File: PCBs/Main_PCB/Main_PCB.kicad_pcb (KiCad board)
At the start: 2 copper layers, 70 x 56 mm, 12 parts, among them J1 LIGHT, J2 OLED, J3 BUTTONS, J4 USB1, J5 USB2, Q1 2N3904, Q2 2N3904, U1 Pico, U2 DS1302, Y1 32.768 KHz

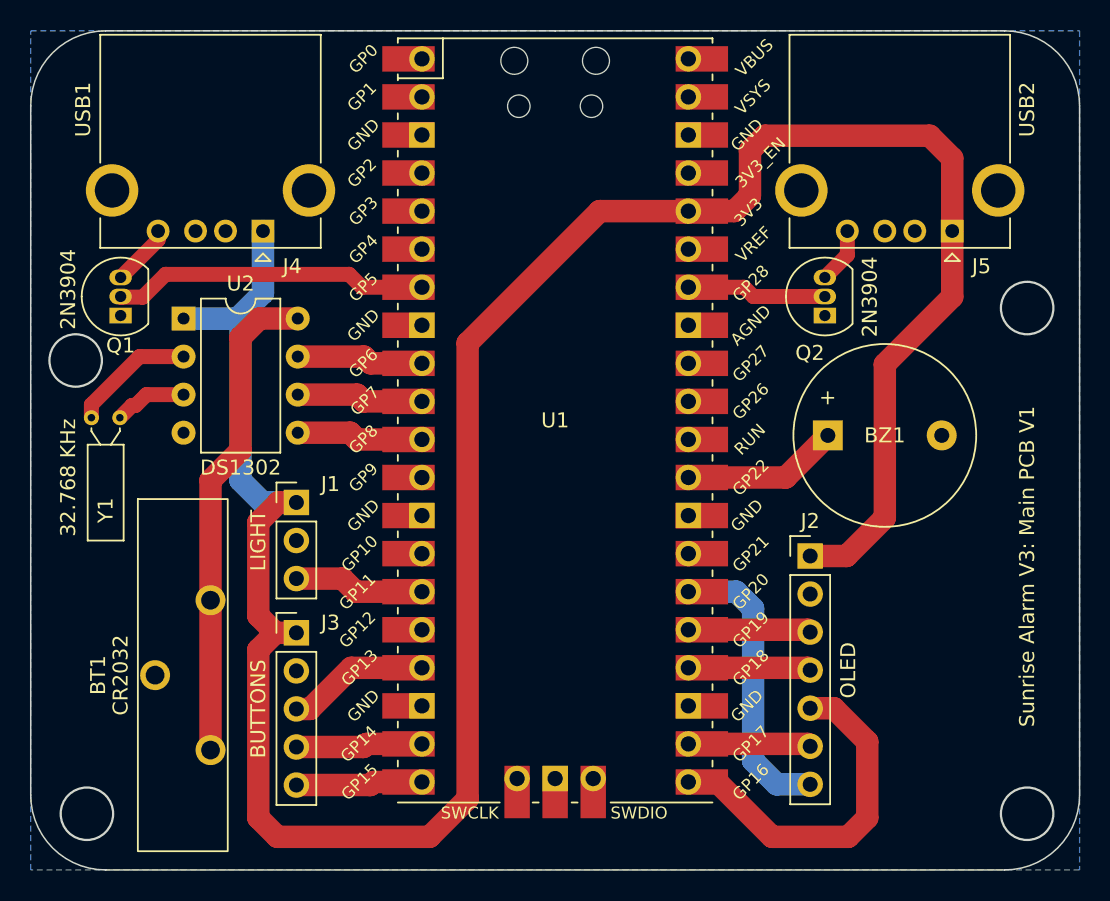
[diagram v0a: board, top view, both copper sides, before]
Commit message: V3.4.1-alpha Added PCB Labels
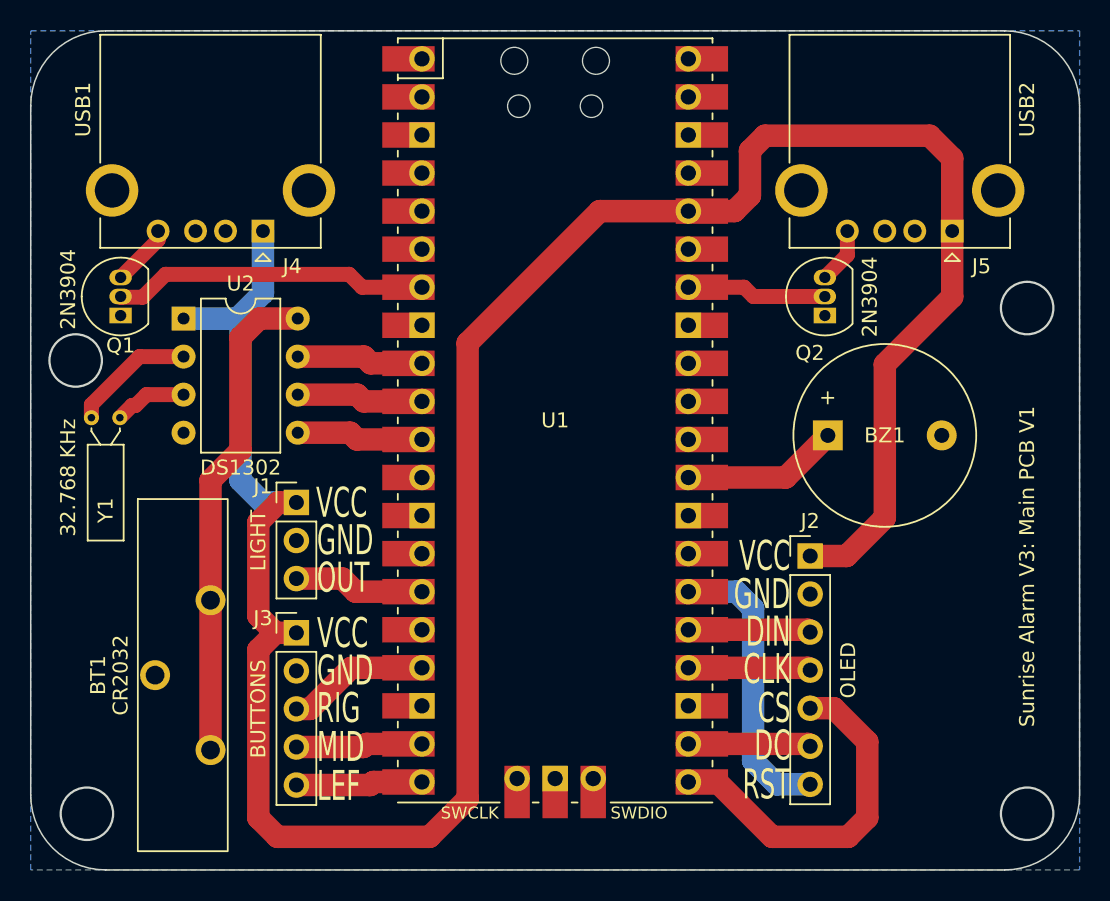
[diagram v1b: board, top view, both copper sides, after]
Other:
- board text added: "CLK"
- board text added: "CS"
- board text added: "DC"
- board text added: "DIN"
- board text added: "GND"
- board text added: "LEF"
- board text added: "MID"
- board text added: "OUT"
- board text added: "RIG"
- board text added: "RST"
- board text added: "VCC"
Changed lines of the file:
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@@
     (property "Sheetname" "")
     (attr through_hole)
-    (fp_text reference "J3" (at 2.27 -0.675) (layer "F.SilkS")
+    (fp_text reference "J3" (at -2.23 -0.975) (layer "F.SilkS")
       (effects (font (size 1 1) (thickness 0.15)))
     )
@@
       (effects (font (size 1 1) (thickness 0.15)))
     )
-    (fp_text user "GP15" (at -13.054 24.13 45) (layer "F.SilkS")
-      (effects (font (size 0.8 0.8) (thickness 0.15)))
-    )
-    (fp_text user "GND" (at 12.8 -19.05 45) (layer "F.SilkS")
-      (effects (font (size 0.8 0.8) (thickness 0.15)))
-    )
-    (fp_text user "GP4" (at -12.8 -11.43 45) (layer "F.SilkS")
-      (effects (font (size 0.8 0.8) (thickness 0.15)))
-    )
-    (fp_text user "GND" (at 12.8 19.05 45) (layer "F.SilkS")
-      (effects (font (size 0.8 0.8) (thickness 0.15)))
-    )
-    (fp_text user "GP28" (at 13.054 -9.144 45) (layer "F.SilkS")
-      (effects (font (size 0.8 0.8) (thickness 0.15)))
-    )
-    (fp_text user "GP18" (at 13.054 16.51 45) (layer "F.SilkS")
-      (effects (font (size 0.8 0.8) (thickness 0.15)))
-    )
-    (fp_text user "RUN" (at 13 1.27 45) (layer "F.SilkS")
-      (effects (font (size 0.8 0.8) (thickness 0.15)))
-    )
-    (fp_text user "GP9" (at -12.8 3.81 45) (layer "F.SilkS")
-      (effects (font (size 0.8 0.8) (thickness 0.15)))
-    )
-    (fp_text user "GP7" (at -12.7 -1.3 45) (layer "F.SilkS")
-      (effects (font (size 0.8 0.8) (thickness 0.15)))
-    )
     (fp_text user "SWDIO" (at 5.6 26.2) (layer "F.SilkS")
       (effects (font (size 0.8 0.8) (thickness 0.15)))
     )
-    (fp_text user "3V3" (at 12.9 -13.9 45) (layer "F.SilkS")
-      (effects (font (size 0.8 0.8) (thickness 0.15)))
-    )
-    (fp_text user "GP27" (at 13.054 -3.8 45) (layer "F.SilkS")
-      (effects (font (size 0.8 0.8) (thickness 0.15)))
-    )
-    (fp_text user "GP22" (at 13.054 3.81 45) (layer "F.SilkS")
-      (effects (font (size 0.8 0.8) (thickness 0.15)))
-    )
-    (fp_text user "GP21" (at 13.054 8.9 45) (layer "F.SilkS")
-      (effects (font (size 0.8 0.8) (thickness 0.15)))
-    )
-    (fp_text user "GP8" (at -12.8 1.27 45) (layer "F.SilkS")
-      (effects (font (size 0.8 0.8) (thickness 0.15)))
-    )
-    (fp_text user "GP5" (at -12.8 -8.89 45) (layer "F.SilkS")
-      (effects (font (size 0.8 0.8) (thickness 0.15)))
-    )
-    (fp_text user "GP20" (at 13.054 11.43 45) (layer "F.SilkS")
-      (effects (font (size 0.8 0.8) (thickness 0.15)))
-    )
-    (fp_text user "GP14" (at -13.1 21.59 45) (layer "F.SilkS")
-      (effects (font (size 0.8 0.8) (thickness 0.15)))
-    )
-    (fp_text user "GND" (at -12.8 -6.35 45) (layer "F.SilkS")
-      (effects (font (size 0.8 0.8) (thickness 0.15)))
-    )
-    (fp_text user "GND" (at -12.8 19.05 45) (layer "F.SilkS")
-      (effects (font (size 0.8 0.8) (thickness 0.15)))
-    )
-    (fp_text user "GP26" (at 13.054 -1.27 45) (layer "F.SilkS")
-      (effects (font (size 0.8 0.8) (thickness 0.15)))
-    )
-    (fp_text user "GP17" (at 13.054 21.59 45) (layer "F.SilkS")
-      (effects (font (size 0.8 0.8) (thickness 0.15)))
-    )
-    (fp_text user "GP1" (at -12.9 -21.6 45) (layer "F.SilkS")
-      (effects (font (size 0.8 0.8) (thickness 0.15)))
-    )
-    (fp_text user "GP16" (at 13.054 24.13 45) (layer "F.SilkS")
-      (effects (font (size 0.8 0.8) (thickness 0.15)))
-    )
-    (fp_text user "3V3_EN" (at 13.7 -17.2 45) (layer "F.SilkS")
-      (effects (font (size 0.8 0.8) (thickness 0.15)))
-    )
-    (fp_text user "GP2" (at -12.9 -16.51 45) (layer "F.SilkS")
-      (effects (font (size 0.8 0.8) (thickness 0.15)))
-    )
-    (fp_text user "GP0" (at -12.8 -24.13 45) (layer "F.SilkS")
-      (effects (font (size 0.8 0.8) (thickness 0.15)))
-    )
-    (fp_text user "GP3" (at -12.8 -13.97 45) (layer "F.SilkS")
-      (effects (font (size 0.8 0.8) (thickness 0.15)))
-    )
-    (fp_text user "GP12" (at -13.2 13.97 45) (layer "F.SilkS")
-      (effects (font (size 0.8 0.8) (thickness 0.15)))
-    )
-    (fp_text user "GND" (at 12.8 6.35 45) (layer "F.SilkS")
-      (effects (font (size 0.8 0.8) (thickness 0.15)))
-    )
     (fp_text user "SWCLK" (at -5.7 26.2) (layer "F.SilkS")
-      (effects (font (size 0.8 0.8) (thickness 0.15)))
-    )
-    (fp_text user "VREF" (at 13.25 -11.75 45) (layer "F.SilkS")
-      (effects (font (size 0.8 0.8) (thickness 0.15)))
-    )
-    (fp_text user "GP10" (at -13.054 8.89 45) (layer "F.SilkS")
-      (effects (font (size 0.8 0.8) (thickness 0.15)))
-    )
-    (fp_text user "GP6" (at -12.8 -3.81 45) (layer "F.SilkS")
-      (effects (font (size 0.8 0.8) (thickness 0.15)))
-    )
-    (fp_text user "GND" (at -12.8 6.35 45) (layer "F.SilkS")
-      (effects (font (size 0.8 0.8) (thickness 0.15)))
-    )
-    (fp_text user "GP19" (at 13.054 13.97 45) (layer "F.SilkS")
-      (effects (font (size 0.8 0.8) (thickness 0.15)))
-    )
-    (fp_text user "GP11" (at -13.2 11.43 45) (layer "F.SilkS")
-      (effects (font (size 0.8 0.8) (thickness 0.15)))
-    )
-    (fp_text user "GND" (at -12.8 -19.05 45) (layer "F.SilkS")
-      (effects (font (size 0.8 0.8) (thickness 0.15)))
-    )
-    (fp_text user "GP13" (at -13.054 16.51 45) (layer "F.SilkS")
-      (effects (font (size 0.8 0.8) (thickness 0.15)))
-    )
-    (fp_text user "VBUS" (at 13.3 -24.2 45) (layer "F.SilkS")
-      (effects (font (size 0.8 0.8) (thickness 0.15)))
-    )
-    (fp_text user "VSYS" (at 13.2 -21.59 45) (layer "F.SilkS")
-      (effects (font (size 0.8 0.8) (thickness 0.15)))
-    )
-    (fp_text user "AGND" (at 13.054 -6.35 45) (layer "F.SilkS")
       (effects (font (size 0.8 0.8) (thickness 0.15)))
     )
@@
     (property "Sheetname" "")
     (attr through_hole)
-    (fp_text reference "J1" (at 2.27 -1.225) (layer "F.SilkS")
+    (fp_text reference "J1" (at -2.23 -1.075) (layer "F.SilkS")
       (effects (font (size 1 1) (thickness 0.15)))
     )
@@
   (gr_line (start 178 49) (end 178 95) (layer "Edge.Cuts") (width 0.1))
   (gr_circle (center 111 66) (end 112.75 66) (layer "Edge.Cuts") (width 0.15) (fill none))
+  (gr_text "GND" (at 127.1 86.7) (layer "F.SilkS")
+    (effects (font (size 2 1.2) (thickness 0.3)) (justify left))
+  )
   (gr_text "Sunrise Alarm V3: Main PCB V1" (at 174.5 79.75 90) (layer "F.SilkS")
     (effects (font (size 1 1) (thickness 0.15)))
   )
+  (gr_text "OUT" (at 127.1 80.5) (layer "F.SilkS")
+    (effects (font (size 2 1.2) (thickness 0.3)) (justify left))
+  )
+  (gr_text "RIG" (at 127.1 89.2) (layer "F.SilkS")
+    (effects (font (size 2 1.2) (thickness 0.3)) (justify left))
+  )
+  (gr_text "CLK" (at 158.7 86.6) (layer "F.SilkS")
+    (effects (font (size 2 1.2) (thickness 0.3)) (justify right))
+  )
+  (gr_text "DC" (at 158.7 91.7) (layer "F.SilkS")
+    (effects (font (size 2 1.2) (thickness 0.3)) (justify right))
+  )
+  (gr_text "RST" (at 158.7 94.3) (layer "F.SilkS")
+    (effects (font (size 2 1.2) (thickness 0.3)) (justify right))
+  )
+  (gr_text "LEF" (at 127.1 94.4) (layer "F.SilkS")
+    (effects (font (size 2 1.2) (thickness 0.3)) (justify left))
+  )
+  (gr_text "CS" (at 158.7 89.2) (layer "F.SilkS")
+    (effects (font (size 2 1.2) (thickness 0.3)) (justify right))
+  )
+  (gr_text "GND" (at 127.1 78) (layer "F.SilkS")
+    (effects (font (size 2 1.2) (thickness 0.3)) (justify left))
+  )
+  (gr_text "DIN" (at 158.7 84.1) (layer "F.SilkS")
+    (effects (font (size 2 1.2) (thickness 0.3)) (justify right))
+  )
+  (gr_text "VCC" (at 127.04 75.5) (layer "F.SilkS")
+    (effects (font (size 2 1.2) (thickness 0.3)) (justify left))
+  )
+  (gr_text "GND" (at 158.69 81.6) (layer "F.SilkS")
+    (effects (font (size 2 1.2) (thickness 0.3)) (justify right))
+  )
+  (gr_text "VCC" (at 127.1 84.2) (layer "F.SilkS")
+    (effects (font (size 2 1.2) (thickness 0.3)) (justify left))
+  )
+  (gr_text "MID" (at 127.1 91.8) (layer "F.SilkS")
+    (effects (font (size 2 1.2) (thickness 0.3)) (justify left))
+  )
+  (gr_text "VCC" (at 158.69 79.0475) (layer "F.SilkS")
+    (effects (font (size 2 1.2) (thickness 0.3)) (justify right))
+  )
   (dimension (type aligned) (layer "Dwgs.User")

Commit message: V3.4.2-alpha Changed Buzzer Footprint
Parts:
- BT1: value CR2032 -> CR2032_Coin_Cell
- BZ1: footprint Buzzer_Beeper:Buzzer_12x9.5RM7.6 -> Buzzer_Beeper:MagneticBuzzer_ProSignal_ABT-410-RC
- U2: value DS1302 -> DS1302+
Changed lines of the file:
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@@
     )
   )
-  (footprint "Buzzer_Beeper:Buzzer_12x9.5RM7.6" (layer "F.Cu")
+  (footprint "Buzzer_Beeper:MagneticBuzzer_ProSignal_ABT-410-RC" (layer "F.Cu")
     (at 161.2 71)
-    (descr "Generic Buzzer, D12mm height 9.5mm with RM7.6mm")
-    (tags "buzzer")
+    (descr "Buzzer, Elektromagnetic Beeper, Summer, 1,5V-DC,")
+    (tags "Pro Signal ABT-410-RC ")
     (property "Sheetfile" "Main_PCB.kicad_sch")
     (property "Sheetname" "")
     (attr through_hole)
-    (fp_text reference "BZ1" (at 3.8 0) (layer "F.SilkS")
-      (effects (font (size 1 1) (thickness 0.15)))
-    )
-    (fp_text value "Buzzer" (at 3.8 7.4) (layer "F.Fab")
-      (effects (font (size 1 1) (thickness 0.15)))
-    )
-    (fp_text user "+" (at -0.01 -2.54) (layer "F.SilkS")
-      (effects (font (size 1 1) (thickness 0.15)))
-    )
-    (fp_text user "+" (at -0.01 -2.54) (layer "F.SilkS")
-      (effects (font (size 1 1) (thickness 0.15)))
-    )
-    (fp_text user "${REFERENCE}" (at 3.8 -4) (layer "F.Fab")
-      (effects (font (size 1 1) (thickness 0.15)))
-    )
-    (fp_circle (center 3.8 0) (end 9.9 0) (layer "F.SilkS") (width 0.12) (fill none))
-    (fp_circle (center 3.8 0) (end 10.05 0) (layer "F.CrtYd") (width 0.05) (fill none))
-    (fp_circle (center 3.8 0) (end 4.8 0) (layer "F.Fab") (width 0.1) (fill none))
-    (fp_circle (center 3.8 0) (end 9.8 0) (layer "F.Fab") (width 0.1) (fill none))
-    (pad "1" thru_hole rect (at 0 0) (size 2 2) (drill 1) (layers *.Cu *.Mask)
+    (fp_text reference "BZ1" (at 3.25 -7) (layer "F.SilkS")
+      (effects (font (size 1 1) (thickness 0.15)))
+    )
+    (fp_text value "Buzzer" (at 3.25 7) (layer "F.Fab")
+      (effects (font (size 1 1) (thickness 0.15)))
+    )
+    (fp_text user "+" (at 0 -1.8) (layer "F.SilkS")
+      (effects (font (size 1 1) (thickness 0.15)))
+    )
+    (fp_text user "${REFERENCE}" (at 3.25 -7) (layer "F.Fab")
+      (effects (font (size 1 1) (thickness 0.15)))
+    )
+    (fp_text user "+" (at 0 -1.8) (layer "F.Fab")
+      (effects (font (size 1 1) (thickness 0.15)))
+    )
+    (fp_circle (center 3.25 0) (end 9.35 0) (layer "F.SilkS") (width 0.12) (fill none))
+    (fp_circle (center 3.25 0) (end 9.5 0) (layer "F.CrtYd") (width 0.05) (fill none))
+    (fp_circle (center 3.25 0) (end 4.4 0) (layer "F.Fab") (width 0.1) (fill none))
+    (fp_circle (center 3.25 0) (end 9.25 0) (layer "F.Fab") (width 0.1) (fill none))
+    (pad "1" thru_hole rect (at 0 0) (size 1.6 1.6) (drill 1) (layers *.Cu *.Mask)
       (net 3 "PWM") (pinfunction "-") (pintype "passive"))
-    (pad "2" thru_hole circle (at 7.6 0) (size 2 2) (drill 1) (layers *.Cu *.Mask)
+    (pad "2" thru_hole circle (at 6.5 0) (size 1.6 1.6) (drill 1) (layers *.Cu *.Mask)
       (net 2 "GND") (pinfunction "+") (pintype "passive"))
-    (model "${KICAD6_3DMODEL_DIR}/Buzzer_Beeper.3dshapes/Buzzer_12x9.5RM7.6.wrl"
+    (model "${KICAD6_3DMODEL_DIR}/Buzzer_Beeper.3dshapes/MagneticBuzzer_ProSignal_ABT-410-RC.wrl"
       (offset (xyz 0 0 0))
       (scale (xyz 1 1 1))
@@
       (effects (font (size 1 1) (thickness 0.15)))
     )
-    (fp_text value "DS1302" (at 3.81 9.95) (layer "F.SilkS")
+    (fp_text value "DS1302+" (at 3.81 9.95) (layer "F.SilkS")
       (effects (font (size 1 1) (thickness 0.15)))
     )
@@
       (effects (font (size 1 1) (thickness 0.15)))
     )
-    (fp_text value "CR2032" (at 0 4.15 90 unlocked) (layer "F.SilkS")
-      (effects (font (size 1 1) (thickness 0.15)))
-    )
+    (fp_text value "CR2032_Coin_Cell" (at 0 4.15 90 unlocked) (layer "F.SilkS")
+      (effects (font (size 1 1) (thickness 0.15)))
+    )
